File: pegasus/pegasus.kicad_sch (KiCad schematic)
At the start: 18 parts, among them IC1 L7805ACV, IC2 RFD900, IC3 L70B-M39, J1 Screw_Terminal_01x04, J2 Screw_Terminal_01x02, U1 Teensy4.0, U2 CON-SMA-EDGE-S, U3 CON-SMA-EDGE-S, U4 XTSD04GCLGEGA

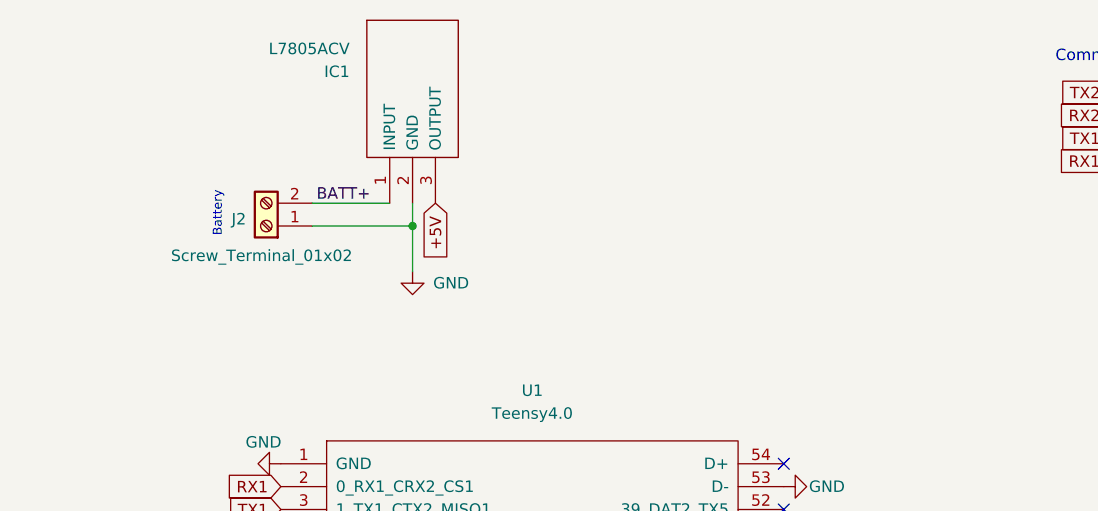
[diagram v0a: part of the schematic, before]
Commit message: New voltage regulator added to schematic and pcb
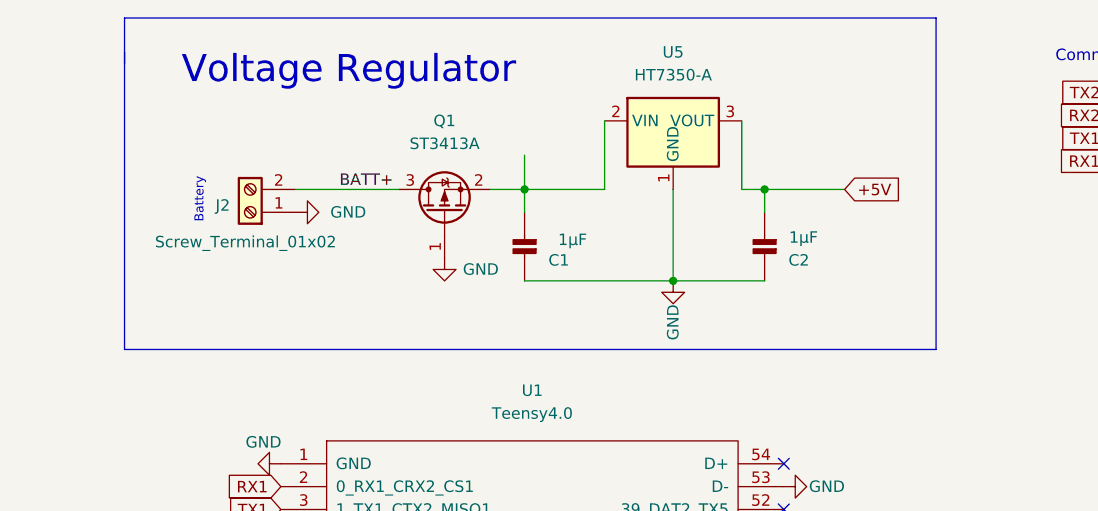
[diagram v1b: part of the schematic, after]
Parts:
- removed IC1: L7805ACV, TO255P460X1020X2008-3P, symbol Voltage Regulator:L7805ACV
- added C1, C2: 1µF, Capacitor_SMD:C_0805_2012Metric_Pad1.18x1.45mm_HandSolder, symbol MPL3115A2_v0.2-eagle-import:CAP_CERAMIC0805-NOOUTLINE
- added Q1: ST3413A, Package_TO_SOT_SMD:SOT-23, symbol Transistor_FET:TSM2301ACX
- added U5: HT7350-A, Package_TO_SOT_SMD:SOT-89-3, symbol Regulator_Linear:HT75xx-1-SOT89
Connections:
- net +5V: now also C2.2, U5.3 (VOUT)
- net BATT+: now also Q1.3 (D)
- net GND: now also C1.1, C2.1, Q1.1 (G), U5.1 (GND)
- new net: C1.2, Q1.2 (S), U5.2 (VIN)
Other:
- note added: "Voltage Regulator"
- moved on the sheet: J2

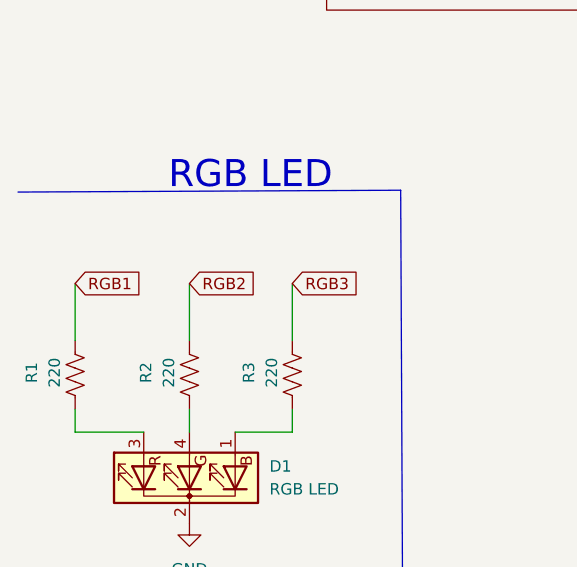
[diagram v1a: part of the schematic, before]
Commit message: Route LED and memory on PCB
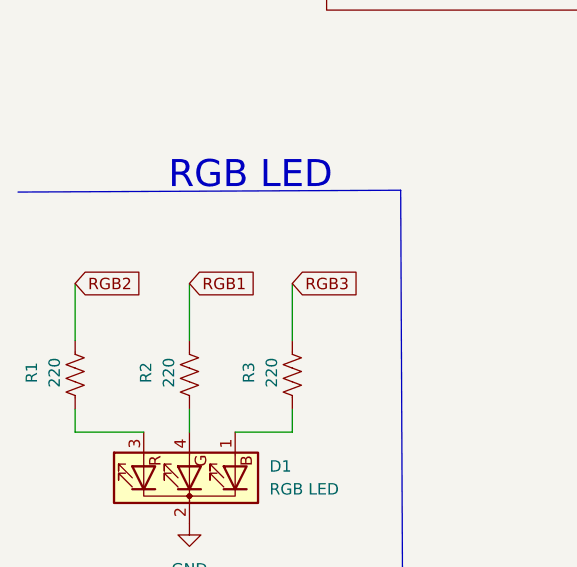
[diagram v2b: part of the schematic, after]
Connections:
- net RGB1: now also R2.2; no longer R1.2
- net RGB2: now also R1.2; no longer R2.2
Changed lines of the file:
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@@
     )
   )
-  (global_label "RGB2" (shape input) (at 31.3436 164.9984 0) (fields_autoplaced)
+  (global_label "RGB1" (shape input) (at 31.3436 164.9984 0) (fields_autoplaced)
     (effects (font (size 1.27 1.27)) (justify left))
     (property "Intersheet References" "${INTERSHEET_REFS}" (id 0) (at 38.7762 164.919 0)
@@
     )
   )
-  (global_label "RGB1" (shape input) (at 18.6436 164.9984 0) (fields_autoplaced)
+  (global_label "RGB2" (shape input) (at 18.6436 164.9984 0) (fields_autoplaced)
     (effects (font (size 1.27 1.27)) (justify left))
     (property "Intersheet References" "${INTERSHEET_REFS}" (id 0) (at 26.0762 164.919 0)
